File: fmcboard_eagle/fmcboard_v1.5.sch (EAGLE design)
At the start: 174 parts, among them IC1 OPA699ID, IC10 LTC6229IMS8E#TRPBF, IC11 7805TV, IC12 SN74AUC2G66DCTR, IC13 SN74AUC2G66DCTR, IC14 SN74AUC2G66DCTR, IC15 SN74AUC2G66DCTR, IC16 DAC7578SPWR, IC17 SN74AUC2G66DCTR, IC18 SN74AUC2G66DCTR, IC19 SN74AUC2G66DCTR, IC2 DAC7578SPWR, IC20 SN74AUC2G66DCTR, IC21 74LVC2G06GW,125, IC22 74LVC2G06GW,125, IC23 74LVC2G06GW,125, IC24 74LVC2G06GW,125, IC3 LTC6229IMS8E#TRPBF, IC4 LTC6229IMS8E#TRPBF, IC5 LM358, IC6 OPA699ID, IC7 OPA699ID, IC8 LTC6229IMS8E#TRPBF, IC9 LTC6229IMS8E#TRPBF, J1 8pin, J10 8pin, J12 4p-2.54, J2 ASP-134604-01, J3 4p-2.54, J4 4p-2.54, J5 8pin, J6 4p-2.54, J7 4p-2.54, J8 4p-2.54, J9 8pin, U1 TXS0108EPWR, U2 STMICROELECTRONICS_L7905ACVST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

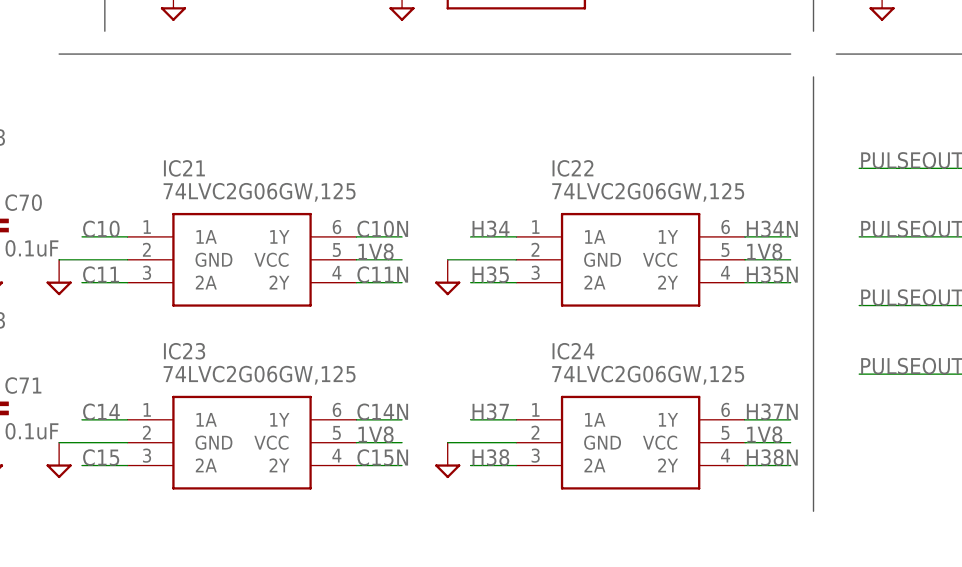
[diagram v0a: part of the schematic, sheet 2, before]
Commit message: Switch to 74AUP2GU04GW inverters
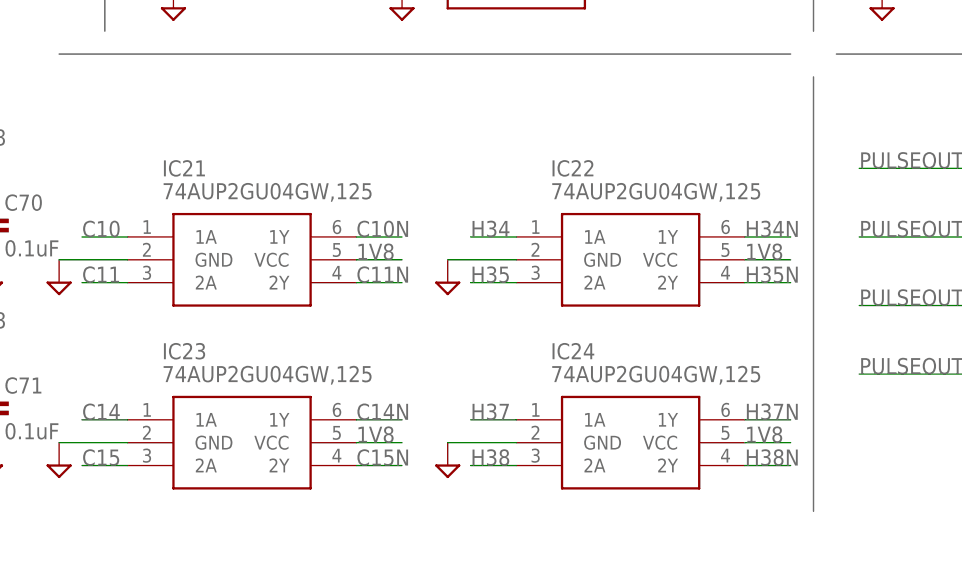
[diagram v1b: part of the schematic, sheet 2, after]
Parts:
- IC21, IC22, IC23, IC24: value 74LVC2G06GW,125 -> 74AUP2GU04GW,125; device 74LVC2G06GW_125:74LVC2G06GW,125 -> 74AUP2GU04GW_125:74AUP2GU04GW,125
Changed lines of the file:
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@@
 <part name="SUPPLY81" library="supply2" library_urn="urn:adsk.eagle:library:372" deviceset="GND" device=""/>
 <part name="SUPPLY82" library="supply2" library_urn="urn:adsk.eagle:library:372" deviceset="GND" device=""/>
-<part name="IC21" library="74LVC2G06GW_125" deviceset="74LVC2G06GW,125" device=""/>
-<part name="IC22" library="74LVC2G06GW_125" deviceset="74LVC2G06GW,125" device=""/>
-<part name="IC23" library="74LVC2G06GW_125" deviceset="74LVC2G06GW,125" device=""/>
-<part name="IC24" library="74LVC2G06GW_125" deviceset="74LVC2G06GW,125" device=""/>
+<part name="IC21" library="74AUP2GU04GW_125" deviceset="74AUP2GU04GW,125" device=""/>
+<part name="IC22" library="74AUP2GU04GW_125" deviceset="74AUP2GU04GW,125" device=""/>
+<part name="IC23" library="74AUP2GU04GW_125" deviceset="74AUP2GU04GW,125" device=""/>
+<part name="IC24" library="74AUP2GU04GW_125" deviceset="74AUP2GU04GW,125" device=""/>
 <part name="SUPPLY83" library="supply2" library_urn="urn:adsk.eagle:library:372" deviceset="GND" device=""/>
 <part name="SUPPLY84" library="supply2" library_urn="urn:adsk.eagle:library:372" deviceset="GND" device=""/>

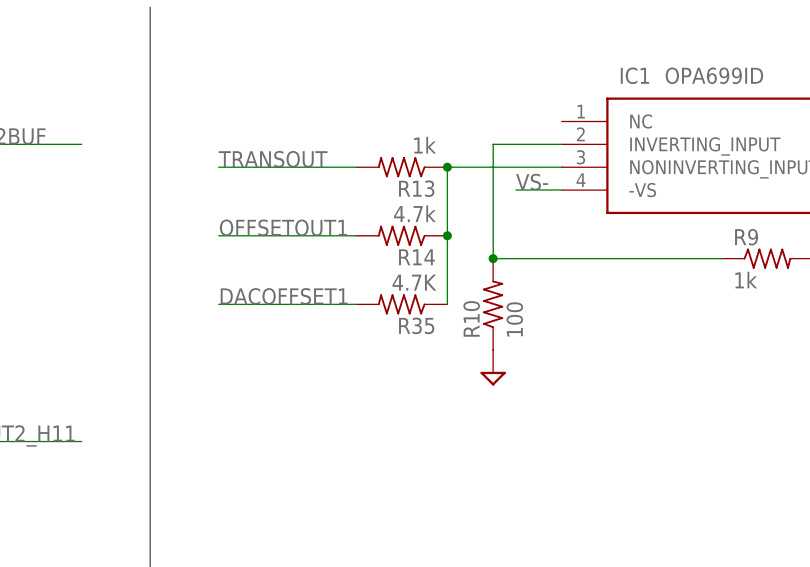
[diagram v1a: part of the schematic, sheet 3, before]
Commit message: Minor BOM update
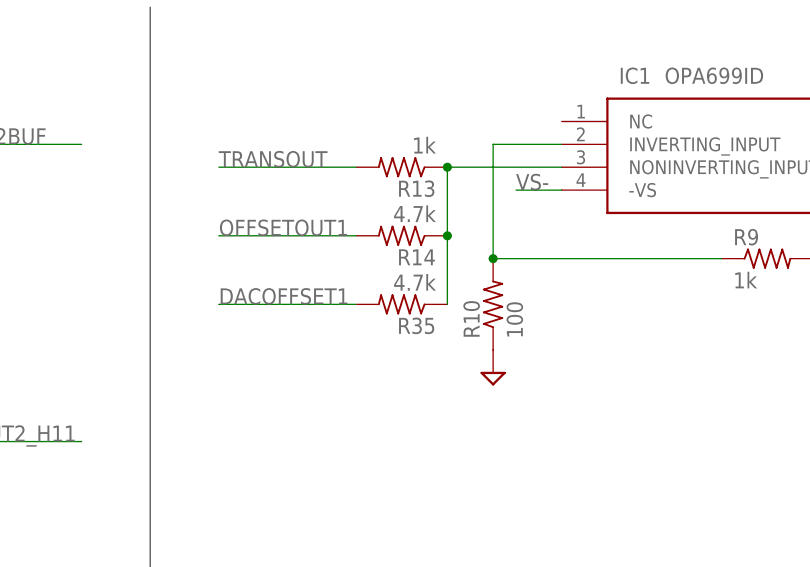
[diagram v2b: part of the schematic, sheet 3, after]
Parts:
- R35: value 4.7K -> 4.7k
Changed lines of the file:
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@@
 <part name="SUPPLY46" library="supply2" library_urn="urn:adsk.eagle:library:372" deviceset="GND" device=""/>
 <part name="R31" library="rcl" library_urn="urn:adsk.eagle:library:334" deviceset="R-US_" device="R0805" package3d_urn="urn:adsk.eagle:package:23553/2" value="4.7k"/>
-<part name="R35" library="rcl" library_urn="urn:adsk.eagle:library:334" deviceset="R-US_" device="R0805" package3d_urn="urn:adsk.eagle:package:23553/2" value="4.7K"/>
+<part name="R35" library="rcl" library_urn="urn:adsk.eagle:library:334" deviceset="R-US_" device="R0805" package3d_urn="urn:adsk.eagle:package:23553/2" value="4.7k"/>
 <part name="J10" library="SparkFun-Connectors" library_urn="urn:adsk.eagle:library:513" deviceset="CONN_08" device="&quot;" package3d_urn="urn:adsk.eagle:package:38138/1" value="8pin"/>
 <part name="C64" library="SparkFun-Passives" deviceset="CAP" device="0805" value="470pF"/>
